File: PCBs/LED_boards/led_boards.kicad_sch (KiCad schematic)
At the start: 14 parts, among them J1 from_shield, J2 from_shield

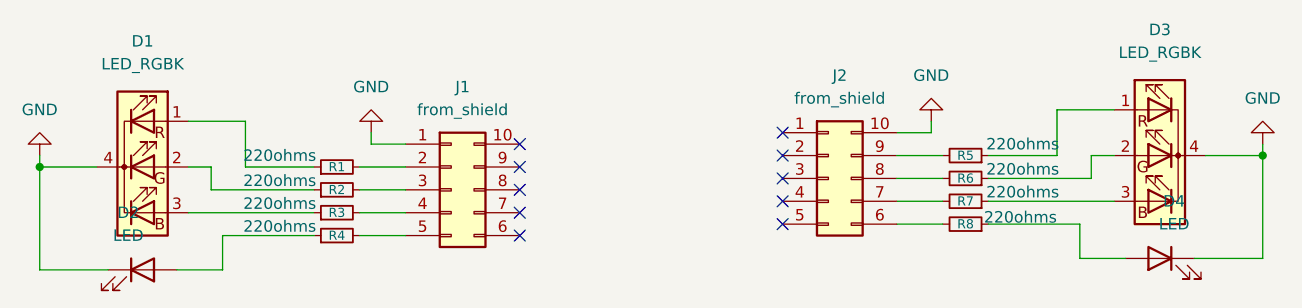
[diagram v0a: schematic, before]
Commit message: create PCBs for easier replication of the system. It has been altered to use an arduino Mega, instead of an arduino Uno.
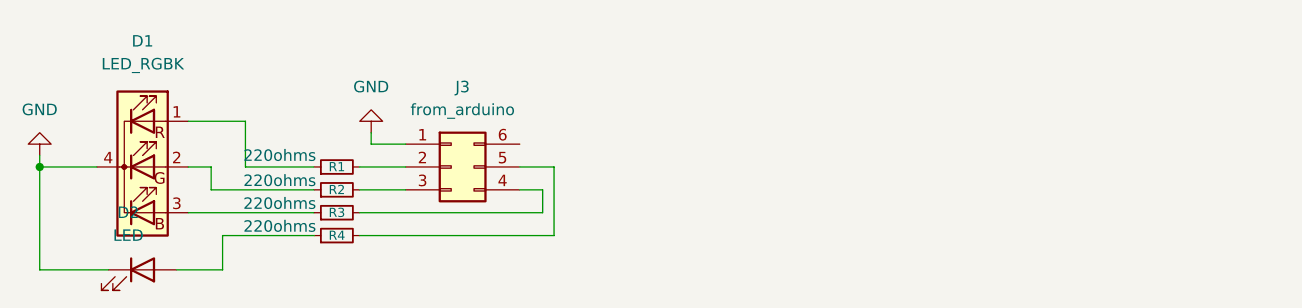
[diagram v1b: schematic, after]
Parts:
- removed D3: LED_RGBK, symbol Device:LED_RGBK
- removed D4: LED, symbol Device:LED
- removed J1, J2: from_shield, symbol Connector_Generic:Conn_02x05_Counter_Clockwise
- removed R5, R6, R7, R8: 220ohms, symbol Device:R_Small
- added J3: from_arduino, Connector_IDC:IDC-Header_2x03_P2.54mm_Vertical, symbol Connector_Generic:Conn_02x03_Counter_Clockwise
- D1: footprint (none) -> LED_THT:LED_D5.0mm-4_RGB_Wide_Pins
- D2: footprint (none) -> LED_THT:LED_D5.0mm_Clear
- R1, R2, R3, R4: footprint (none) -> Resistor_THT:R_Axial_DIN0309_L9.0mm_D3.2mm_P12.70mm_Horizontal
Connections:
- net GND: now also J3.1 (Pin_1)
- net at R2.2: now also J3.3 (Pin_3)
- net at R1.2: now also J3.2 (Pin_2)
- net at R3.2: now also J3.4 (Pin_4)
- net at R4.2: now also J3.5 (Pin_5)
- no-connect marks 10 -> 0
